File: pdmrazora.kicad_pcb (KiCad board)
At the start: 2 copper layers, 174 x 202 mm, 54 parts, among them J1 6473418-1, J2 M6_VBAT, J3 M6_GND, M1000 Module:mega-mcu144/0.7, U1 BTS50010-1TAD, U11 BTS7004-1EPP, U12 BTS7004-1EPP, U13 BTS7004-1EPP, U14 BTS7004-1EPP, U15 BTS7004-1EPP, U16 BTS7004-1EPP, U17 BTS7004-1EPP, U18 BTS7004-1EPP, U2 BTS50010-1TAD, U3 BTS50010-1TAD, U4 BTS50010-1TAD

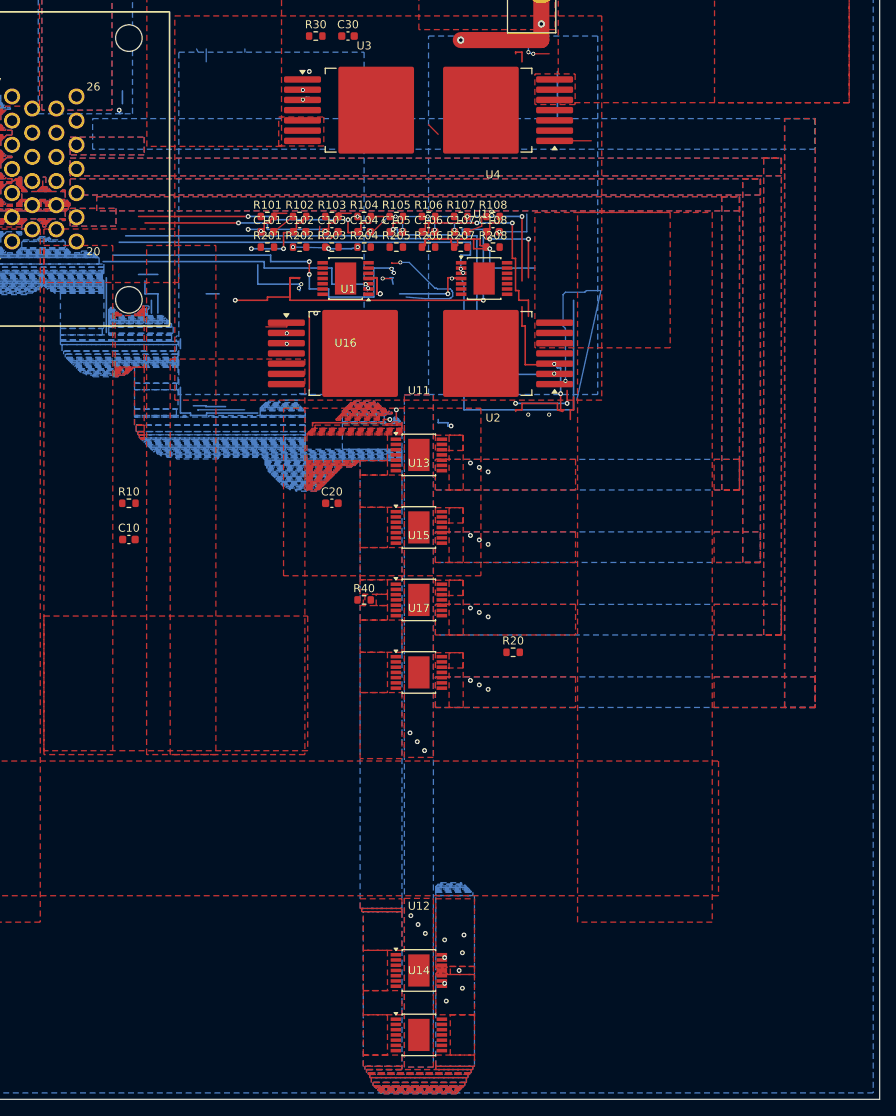
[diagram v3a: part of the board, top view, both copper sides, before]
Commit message: Pour ADIO4/6/8 at board-wide 2 oz so the 8 A necks clear 1.74 mm.
IPC-2221A external 20 C at 2 oz is 1.74 mm for 8 A and 8.36 mm for 25 A.
HP pours stay at the 16.72 mm class. Odd pin sections are narrowed only
where a 1.74 mm even throat cannot share the 3.0 mm SuperSeal pitch.

Co-authored-by: Quintin <quintinbannink42@users.noreply.github.com>
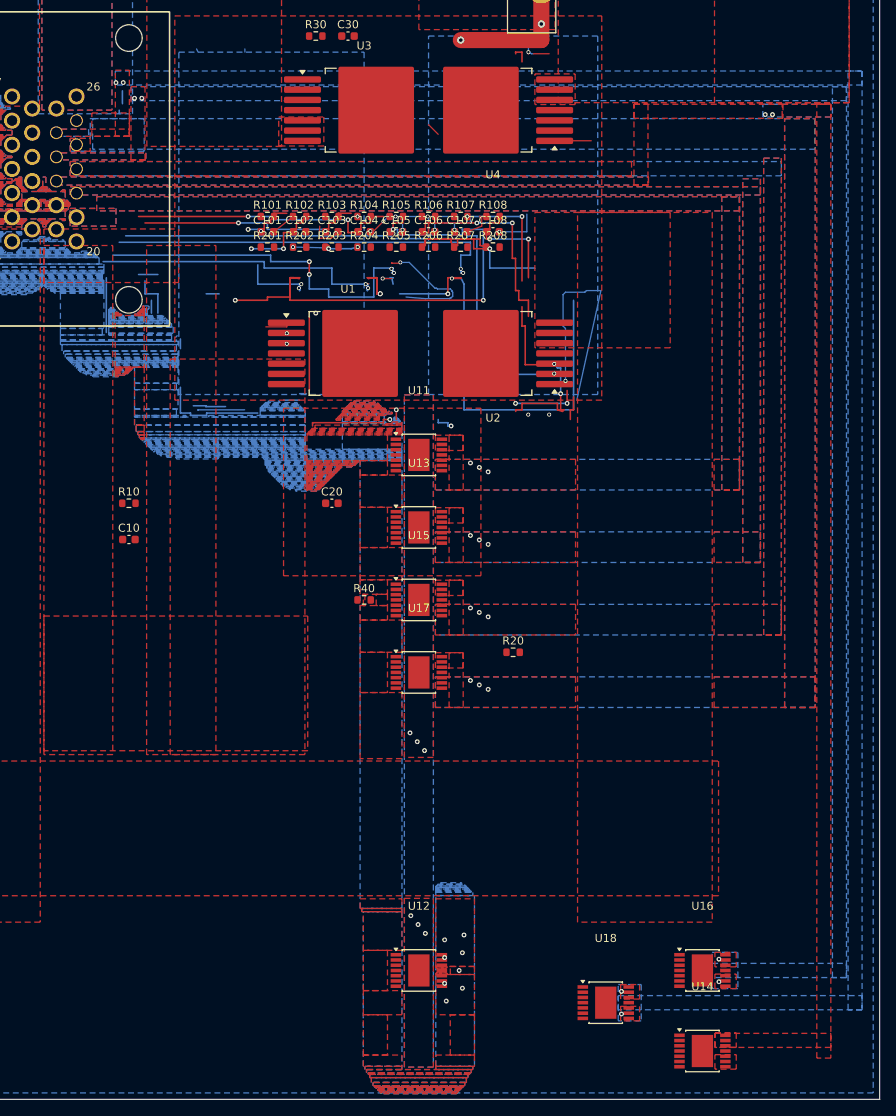
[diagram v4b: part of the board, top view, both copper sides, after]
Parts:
- moved U16 96.7 mm to (120.0, 146.0), turned to 0 degrees
- moved U18 91.2 mm to (108.0, 150.0)
- moved U14 35.3 mm to (120.0, 156.0)
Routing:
- net IN_AUX4: track 7.86 -> 2.26 mm
- net GND: track 112.5 -> 110.9 mm, vias 16 -> 15
- net IN_AUX3: track 17.9 -> 16.9 mm, vias 3 -> 1
- net OUT_PWM3: track 1.88 -> 1.66 mm, vias 1 -> 0
- net OUT_PWM4: vias 1 -> 0
- net ADIO8: vias 0 -> 4
- net ADIO6: vias 0 -> 4
- net ADIO4: vias 0 -> 2
- added copper zone on B.Cu, net ADIO4
- added copper zone on F.Cu, net ADIO4
- added copper zone on B.Cu, net ADIO6
- added copper zone on F.Cu, net ADIO6
- added copper zone on B.Cu, net ADIO8
- added copper zone on F.Cu, net ADIO8
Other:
- board text added: "FAB stackup 2 oz (70 um) F.Cu + 2 oz B.Cu, core 1.46 mm, 1.6 mm finished. IPC-2221A external 20 C: 8 A = 1.74 mm, 25 A = 8.36 mm. Copper weight is board-wide."

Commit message: Reconnect U14/U16/U18 and the even-channel sense taps.
VBAT, GND, EN, and IS land on the moved drivers, and R204/R206/R208 tap ADIO4/6/8. Unconnected goes from 174 to 158. Hard DRC stays 0. The 2 oz series necks are unchanged.

Co-authored-by: Quintin <quintinbannink42@users.noreply.github.com>
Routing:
- net IN_RES3: track 70.9 -> 574.8 mm, vias 4 -> 5
- net IN_RES1: track 45.8 -> 536.8 mm, vias 6 -> 7
- net IN_O2S: track 44.2 -> 517.0 mm, vias 2 -> 3
- net OUT_PWM8: track 0.00 -> 466.8 mm, vias 0 -> 2
- net OUT_IO8: track 50.4 -> 515.0 mm, vias 2 -> 4
- net OUT_IO6: track 38.7 -> 482.6 mm, vias 2 -> 4
- net ADIO8: track 0.00 -> 141.7 mm, vias 4 -> 5
- net ADIO4: track 0.00 -> 129.2 mm, vias 2 -> 4
- net ADIO6: track 0.00 -> 110.9 mm, vias 4 -> 7
- net GND: track 110.9 -> 116.2 mm, vias 15 -> 18
- net VBAT: vias 10 -> 16

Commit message: Close leftover rats and restore ADIO5/ADIO8 2 oz necks (#27)
Jeoff thin-review MERGE. Hard DRC 0; unconnected 158→141; ADIO5 1.83 mm / ADIO8 drop 1.77 mm. ADIO2/HP/Razor loom untouched. Create-board CI still fails pre-existing pdmrazor vs pdmrazora naming (same as #26+); not a board regression.
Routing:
- net GND: track 116.2 -> 162.7 mm, vias 18 -> 19
- net VBAT: track 43.9 -> 68.9 mm
- net SENSOR_5V: track 224.5 -> 237.9 mm, vias 8 -> 9
- net IN_AUX1: track 1.09 -> 11.0 mm
- net IN_VIGN: track 1.81 -> 9.03 mm
- net SENSOR_GND: track 92.4 -> 95.8 mm
- net OUT_PWM6: track 0.80 -> 1.45 mm
- net OUT_IO7: track 46.0 -> 46.6 mm
- net OUT_IO5: track 36.0 -> 36.7 mm
- net OUT_PWM5: track 0.80 -> 1.45 mm
- net OUT_PWM7: track 2.00 -> 2.65 mm
